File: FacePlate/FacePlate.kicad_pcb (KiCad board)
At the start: 4 copper layers, 131.1 x 44 mm, 50 parts, among them J2 GPIO, J3 Conn_01x04_Pin, U4 SX1280, U5 MCP2515-xST, U6 MCP2551-I-SN, U7 AMS1117-3.3, Y2 ABM3-8.000MHZ-D2Y-T

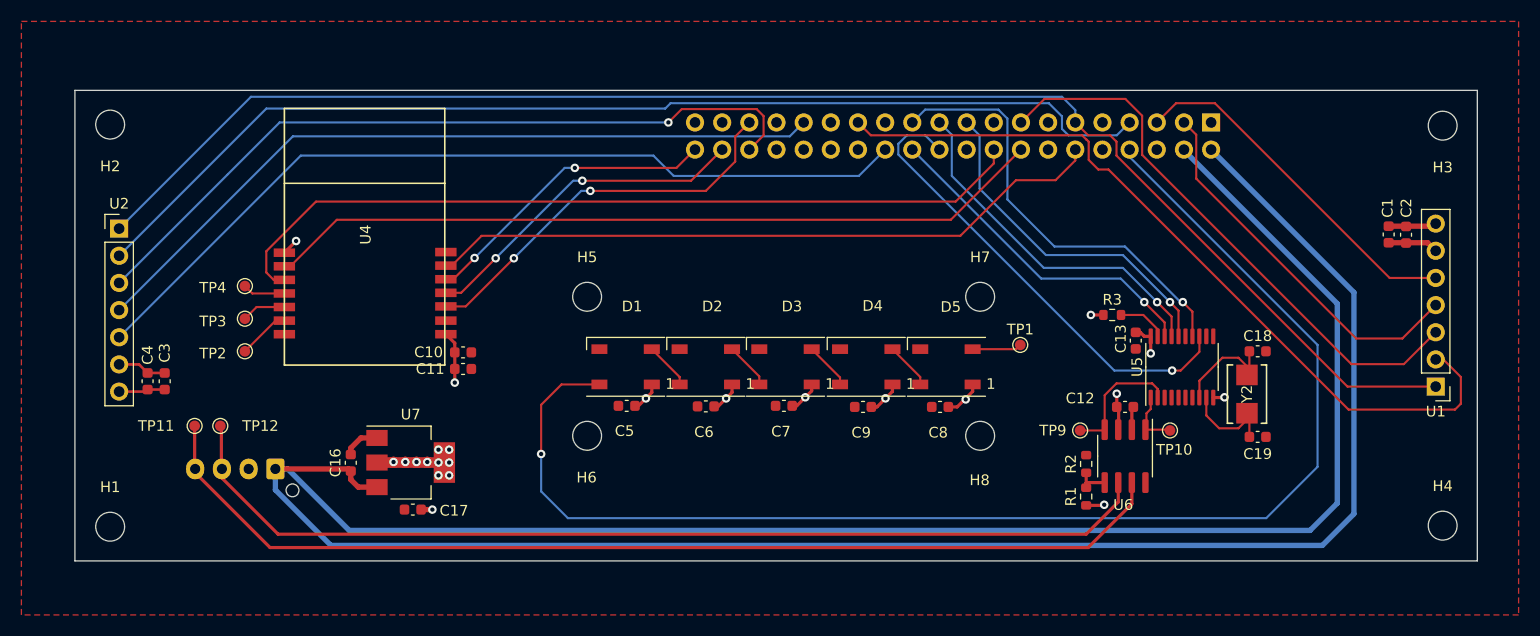
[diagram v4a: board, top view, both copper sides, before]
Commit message: update radio model
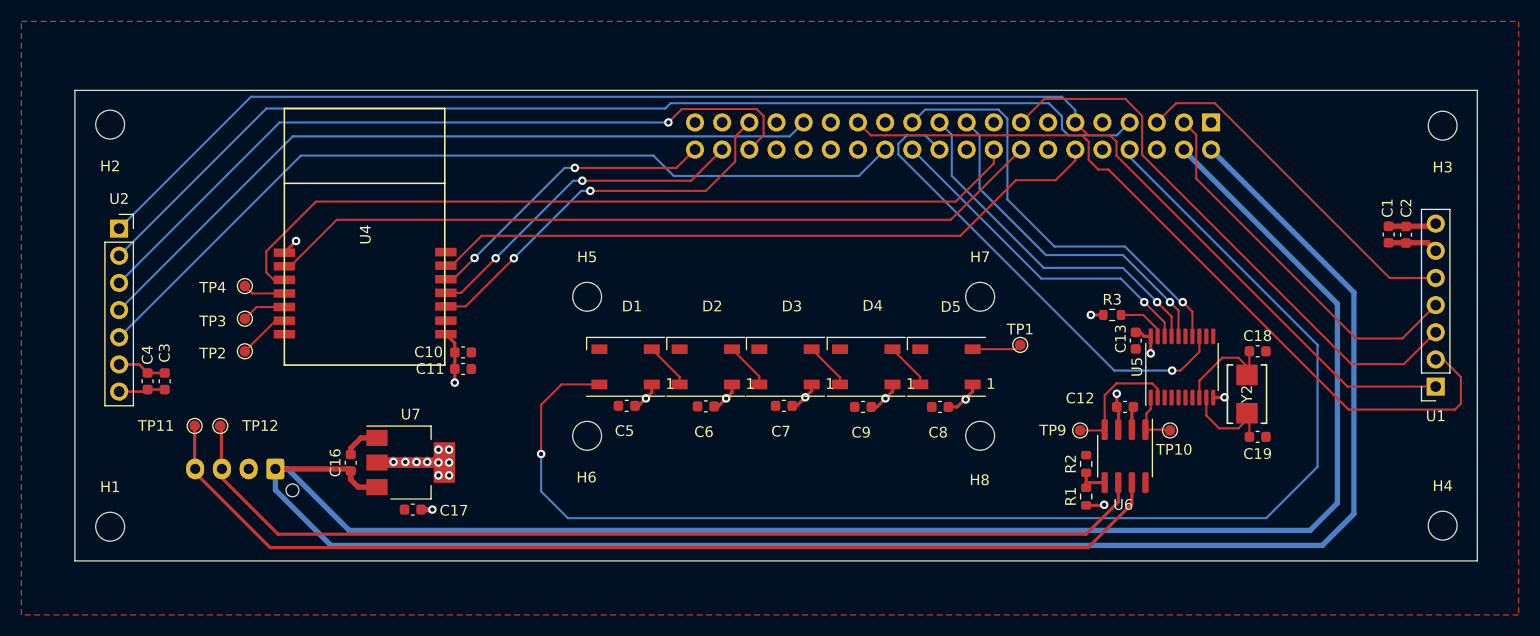
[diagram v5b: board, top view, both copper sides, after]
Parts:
- U1, U2: footprint Connector_PinHeader_2.54mm:PinHeader_1x07_P2.54mm_Vertical -> Connector_PinSocket_2.54mm:PinSocket_1x07_P2.54mm_Vertical
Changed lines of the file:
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@@
   (net 57 "/CAN/OSC2")
   (net 58 "/CAN/OSC1")
-  (footprint "Connector_PinHeader_2.54mm:PinHeader_1x07_P2.54mm_Vertical" (layer "F.Cu")
+  (footprint "Connector_PinSocket_2.54mm:PinSocket_1x07_P2.54mm_Vertical" (layer "F.Cu")
     (at 104.14 68.9256)
-    (descr "Through hole straight pin header, 1x07, 2.54mm pitch, single row")
-    (tags "Through hole pin header THT 1x07 2.54mm single row")
+    (descr "Through hole straight socket strip, 1x07, 2.54mm pitch, single row (from Kicad 4.0.7), script generated")
+    (tags "Through hole socket strip THT 1x07 2.54mm single row")
     (property "LCSC" "C718238")
     (property "Sheetfile" "FacePlate.kicad_sch")
     (property "Sheetname" "")
     (attr through_hole)
-    (fp_text reference "U2" (at 0 -2.33) (layer "F.SilkS")
-        (effects (font (size 1 1) (thickness 0.15)))
-    )
-    (fp_text value "~" (at 0 17.57) (layer "F.Fab")
+    (fp_text reference "U2" (at 0 -2.77) (layer "F.SilkS")
+        (effects (font (size 1 1) (thickness 0.15)))
+    )
+    (fp_text value "~" (at 0 18.01) (layer "F.Fab")
         (effects (font (size 1 1) (thickness 0.15)))
     )
@@
         (effects (font (size 1 1) (thickness 0.15)))
     )
-    (fp_line (start -1.33 -1.33) (end 0 -1.33)
-      (stroke (width 0.12) (type solid)) (layer "F.SilkS"))
-    (fp_line (start -1.33 0) (end -1.33 -1.33)
-      (stroke (width 0.12) (type solid)) (layer "F.SilkS"))
     (fp_line (start -1.33 1.27) (end -1.33 16.57)
       (stroke (width 0.12) (type solid)) (layer "F.SilkS"))
@@
     (fp_line (start -1.33 16.57) (end 1.33 16.57)
       (stroke (width 0.12) (type solid)) (layer "F.SilkS"))
+    (fp_line (start 0 -1.33) (end 1.33 -1.33)
+      (stroke (width 0.12) (type solid)) (layer "F.SilkS"))
+    (fp_line (start 1.33 -1.33) (end 1.33 0)
+      (stroke (width 0.12) (type solid)) (layer "F.SilkS"))
     (fp_line (start 1.33 1.27) (end 1.33 16.57)
       (stroke (width 0.12) (type solid)) (layer "F.SilkS"))
-    (fp_line (start -1.8 -1.8) (end -1.8 17.05)
-      (stroke (width 0.05) (type solid)) (layer "F.CrtYd"))
-    (fp_line (start -1.8 17.05) (end 1.8 17.05)
-      (stroke (width 0.05) (type solid)) (layer "F.CrtYd"))
-    (fp_line (start 1.8 -1.8) (end -1.8 -1.8)
-      (stroke (width 0.05) (type solid)) (layer "F.CrtYd"))
-    (fp_line (start 1.8 17.05) (end 1.8 -1.8)
-      (stroke (width 0.05) (type solid)) (layer "F.CrtYd"))
-    (fp_line (start -1.27 -0.635) (end -0.635 -1.27)
-      (stroke (width 0.1) (type solid)) (layer "F.Fab"))
-    (fp_line (start -1.27 16.51) (end -1.27 -0.635)
-      (stroke (width 0.1) (type solid)) (layer "F.Fab"))
-    (fp_line (start -0.635 -1.27) (end 1.27 -1.27)
-      (stroke (width 0.1) (type solid)) (layer "F.Fab"))
-    (fp_line (start 1.27 -1.27) (end 1.27 16.51)
+    (fp_line (start -1.8 -1.8) (end 1.75 -1.8)
+      (stroke (width 0.05) (type solid)) (layer "F.CrtYd"))
+    (fp_line (start -1.8 17) (end -1.8 -1.8)
+      (stroke (width 0.05) (type solid)) (layer "F.CrtYd"))
+    (fp_line (start 1.75 -1.8) (end 1.75 17)
+      (stroke (width 0.05) (type solid)) (layer "F.CrtYd"))
+    (fp_line (start 1.75 17) (end -1.8 17)
+      (stroke (width 0.05) (type solid)) (layer "F.CrtYd"))
+    (fp_line (start -1.27 -1.27) (end 0.635 -1.27)
+      (stroke (width 0.1) (type solid)) (layer "F.Fab"))
+    (fp_line (start -1.27 16.51) (end -1.27 -1.27)
+      (stroke (width 0.1) (type solid)) (layer "F.Fab"))
+    (fp_line (start 0.635 -1.27) (end 1.27 -0.635)
+      (stroke (width 0.1) (type solid)) (layer "F.Fab"))
+    (fp_line (start 1.27 -0.635) (end 1.27 16.51)
       (stroke (width 0.1) (type solid)) (layer "F.Fab"))
     (fp_line (start 1.27 16.51) (end -1.27 16.51)
@@
     (pad "7" thru_hole oval (at 0 15.24) (size 1.7 1.7) (drill 1) (layers "*.Cu" "*.Mask")
       (net 3 "+3.3V") (pinfunction "VCC") (pintype "power_in"))
-    (model "${KICAD6_3DMODEL_DIR}/Connector_PinHeader_2.54mm.3dshapes/PinHeader_1x07_P2.54mm_Vertical.wrl"
+    (model "${KICAD6_3DMODEL_DIR}/Connector_PinSocket_2.54mm.3dshapes/PinSocket_1x07_P2.54mm_Vertical.wrl"
       (offset (xyz 0 0 0))
       (scale (xyz 1 1 1))
@@
     )
   )
-  (footprint "Connector_PinHeader_2.54mm:PinHeader_1x07_P2.54mm_Vertical" (layer "F.Cu")
+  (footprint "Connector_PinSocket_2.54mm:PinSocket_1x07_P2.54mm_Vertical" (layer "F.Cu")
     (at 227.25 83.7 180)
-    (descr "Through hole straight pin header, 1x07, 2.54mm pitch, single row")
-    (tags "Through hole pin header THT 1x07 2.54mm single row")
+    (descr "Through hole straight socket strip, 1x07, 2.54mm pitch, single row (from Kicad 4.0.7), script generated")
+    (tags "Through hole socket strip THT 1x07 2.54mm single row")
     (property "LCSC" "C718238")
     (property "Sheetfile" "FacePlate.kicad_sch")
     (property "Sheetname" "")
     (attr through_hole)
-    (fp_text reference "U1" (at 0 -2.33) (layer "F.SilkS")
-        (effects (font (size 1 1) (thickness 0.15)))
-    )
-    (fp_text value "~" (at 0 17.57) (layer "F.Fab")
-        (effects (font (size 1 1) (thickness 0.15)))
-    )
-    (fp_text user "${REFERENCE}" (at 0 7.62 90) (layer "F.Fab")
-        (effects (font (size 1 1) (thickness 0.15)))
-    )
-    (fp_line (start -1.33 -1.33) (end 0 -1.33)
-      (stroke (width 0.12) (type solid)) (layer "F.SilkS"))
-    (fp_line (start -1.33 0) (end -1.33 -1.33)
-      (stroke (width 0.12) (type solid)) (layer "F.SilkS"))
+    (fp_text reference "U1" (at 0 -2.77 180) (layer "F.SilkS")
+        (effects (font (size 1 1) (thickness 0.15)))
+    )
+    (fp_text value "~" (at 0 18.01 180) (layer "F.Fab")
+        (effects (font (size 1 1) (thickness 0.15)))
+    )
+    (fp_text user "${REFERENCE}" (at 0 7.62 270) (layer "F.Fab")
+        (effects (font (size 1 1) (thickness 0.15)))
+    )
     (fp_line (start -1.33 1.27) (end -1.33 16.57)
       (stroke (width 0.12) (type solid)) (layer "F.SilkS"))
@@
     (fp_line (start -1.33 16.57) (end 1.33 16.57)
       (stroke (width 0.12) (type solid)) (layer "F.SilkS"))
+    (fp_line (start 0 -1.33) (end 1.33 -1.33)
+      (stroke (width 0.12) (type solid)) (layer "F.SilkS"))
+    (fp_line (start 1.33 -1.33) (end 1.33 0)
+      (stroke (width 0.12) (type solid)) (layer "F.SilkS"))
     (fp_line (start 1.33 1.27) (end 1.33 16.57)
       (stroke (width 0.12) (type solid)) (layer "F.SilkS"))
-    (fp_line (start -1.8 -1.8) (end -1.8 17.05)
-      (stroke (width 0.05) (type solid)) (layer "F.CrtYd"))
-    (fp_line (start -1.8 17.05) (end 1.8 17.05)
-      (stroke (width 0.05) (type solid)) (layer "F.CrtYd"))
-    (fp_line (start 1.8 -1.8) (end -1.8 -1.8)
-      (stroke (width 0.05) (type solid)) (layer "F.CrtYd"))
-    (fp_line (start 1.8 17.05) (end 1.8 -1.8)
-      (stroke (width 0.05) (type solid)) (layer "F.CrtYd"))
-    (fp_line (start -1.27 -0.635) (end -0.635 -1.27)
-      (stroke (width 0.1) (type solid)) (layer "F.Fab"))
-    (fp_line (start -1.27 16.51) (end -1.27 -0.635)
-      (stroke (width 0.1) (type solid)) (layer "F.Fab"))
-    (fp_line (start -0.635 -1.27) (end 1.27 -1.27)
-      (stroke (width 0.1) (type solid)) (layer "F.Fab"))
-    (fp_line (start 1.27 -1.27) (end 1.27 16.51)
+    (fp_line (start -1.8 -1.8) (end 1.75 -1.8)
+      (stroke (width 0.05) (type solid)) (layer "F.CrtYd"))
+    (fp_line (start -1.8 17) (end -1.8 -1.8)
+      (stroke (width 0.05) (type solid)) (layer "F.CrtYd"))
+    (fp_line (start 1.75 -1.8) (end 1.75 17)
+      (stroke (width 0.05) (type solid)) (layer "F.CrtYd"))
+    (fp_line (start 1.75 17) (end -1.8 17)
+      (stroke (width 0.05) (type solid)) (layer "F.CrtYd"))
+    (fp_line (start -1.27 -1.27) (end 0.635 -1.27)
+      (stroke (width 0.1) (type solid)) (layer "F.Fab"))
+    (fp_line (start -1.27 16.51) (end -1.27 -1.27)
+      (stroke (width 0.1) (type solid)) (layer "F.Fab"))
+    (fp_line (start 0.635 -1.27) (end 1.27 -0.635)
+      (stroke (width 0.1) (type solid)) (layer "F.Fab"))
+    (fp_line (start 1.27 -0.635) (end 1.27 16.51)
       (stroke (width 0.1) (type solid)) (layer "F.Fab"))
     (fp_line (start 1.27 16.51) (end -1.27 16.51)
@@
     (pad "7" thru_hole oval (at 0 15.24 180) (size 1.7 1.7) (drill 1) (layers "*.Cu" "*.Mask")
       (net 3 "+3.3V") (pinfunction "VCC") (pintype "power_in"))
-    (model "${KICAD6_3DMODEL_DIR}/Connector_PinHeader_2.54mm.3dshapes/PinHeader_1x07_P2.54mm_Vertical.wrl"
+    (model "${KICAD6_3DMODEL_DIR}/Connector_PinSocket_2.54mm.3dshapes/PinSocket_1x07_P2.54mm_Vertical.wrl"
       (offset (xyz 0 0 0))
       (scale (xyz 1 1 1))
@@
     (pad "14" smd rect (at -9.31 -7.6 90) (size 0.8 2) (layers "F.Cu" "F.Paste" "F.Mask")
       (net 1 "GND") (pinfunction "GND") (pintype "power_in"))
+    (model "${KIPRJMOD}/3d_models/E28-2G4M27S.STEP"
+      (offset (xyz 0 26.5 3))
+      (scale (xyz 1 1 1))
+      (rotate (xyz -90 0 0))
+    )
   )
   (footprint "Resistor_SMD:R_0603_1608Metric" (layer "F.Cu")

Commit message: finalize with 0ohms
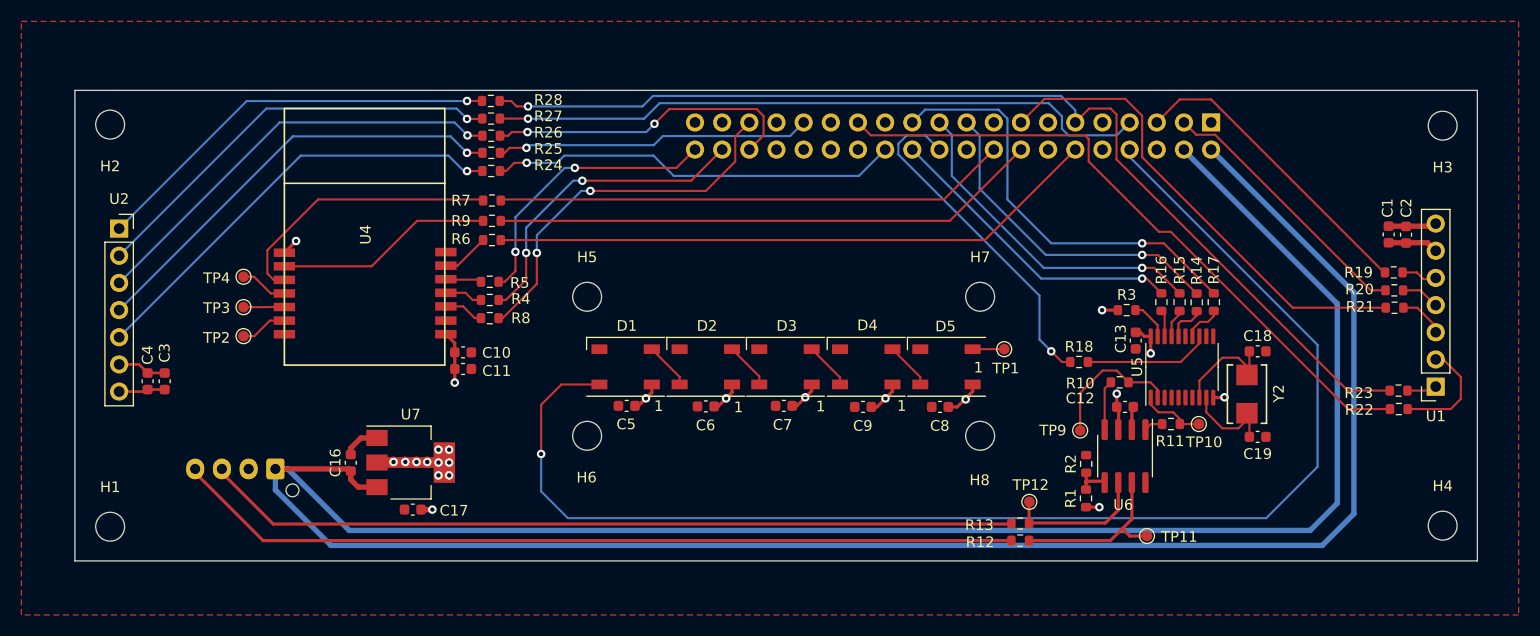
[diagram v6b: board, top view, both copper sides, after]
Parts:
- added R10: 0k, Resistor_SMD:R_0603_1608Metric, F.Cu at (197.7, 83.3)
- added R11: 0k, Resistor_SMD:R_0603_1608Metric, F.Cu at (202.5, 87.2)
- added R12: 0k, Resistor_SMD:R_0603_1608Metric, F.Cu at (188.4, 98.1)
- added R13: 0k, Resistor_SMD:R_0603_1608Metric, F.Cu at (188.4, 96.5)
- added R14: 0k, Resistor_SMD:R_0603_1608Metric, F.Cu at (204.9, 75.8)
- added R15: 0k, Resistor_SMD:R_0603_1608Metric, F.Cu at (203.3, 75.8)
- added R16: 0k, Resistor_SMD:R_0603_1608Metric, F.Cu at (201.6, 75.8)
- added R17: 0k, Resistor_SMD:R_0603_1608Metric, F.Cu at (206.5, 75.8)
- added R18: 0k, Resistor_SMD:R_0603_1608Metric, F.Cu at (193.9, 81.4)
- added R19: 0k, Resistor_SMD:R_0603_1608Metric, F.Cu at (223.3, 73.0)
- added R20: 0k, Resistor_SMD:R_0603_1608Metric, F.Cu at (223.4, 74.7)
- added R21: 0k, Resistor_SMD:R_0603_1608Metric, F.Cu at (223.4, 76.3)
- added R22: 0k, Resistor_SMD:R_0603_1608Metric, F.Cu at (223.8, 85.8)
- added R23: 0k, Resistor_SMD:R_0603_1608Metric, F.Cu at (223.8, 84.1)
- added R24: 0k, Resistor_SMD:R_0603_1608Metric, F.Cu at (138.9, 63.5)
- added R25: 0k, Resistor_SMD:R_0603_1608Metric, F.Cu at (138.9, 61.8)
- added R26: 0k, Resistor_SMD:R_0603_1608Metric, F.Cu at (138.9, 60.2)
- added R27: 0k, Resistor_SMD:R_0603_1608Metric, F.Cu at (138.9, 58.6)
- added R28: 0k, Resistor_SMD:R_0603_1608Metric, F.Cu at (138.9, 57.0)
- added R4: 0k, Resistor_SMD:R_0603_1608Metric, F.Cu at (138.8, 75.6)
- added R5: 0k, Resistor_SMD:R_0603_1608Metric, F.Cu at (138.8, 73.9)
- added R6: 0k, Resistor_SMD:R_0603_1608Metric, F.Cu at (139.0, 70.0)
- added R7: 0k, Resistor_SMD:R_0603_1608Metric, F.Cu at (139.0, 66.3)
- added R8: 0k, Resistor_SMD:R_0603_1608Metric, F.Cu at (138.8, 77.3)
- added R9: 0k, Resistor_SMD:R_0603_1608Metric, F.Cu at (139.0, 68.2)
- moved TP11 89.6 mm to (200.2, 97.7)
- moved TP12 76.0 mm to (189.2, 94.5)
- moved TP10 2.77 mm to (205.1, 87.2)
- moved TP1 1.55 mm to (186.9, 80.2)
- moved TP2 1.43 mm to (115.8, 79.0)
- moved R3 1.42 mm to (198.3, 76.5)
- moved TP3 1.09 mm to (115.8, 76.3)
- moved TP4 0.88 mm to (115.8, 73.4)
- moved R1 0.17 mm to (194.6, 94.2)
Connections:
- TP11 pad 1: /CAN/CAN_H -> Net-(U6-CANH)
- TP12 pad 1: /CAN/CAN_L -> Net-(U6-CANL)
- U1 pad 1: /GPIO[17] -> Net-(U1-RST)
- U1 pad 2: /SPI3_NSS -> Net-(U1-CS)
- U1 pad 3: /GPIO[22] -> Net-(U1-DC)
- U1 pad 4: /SPI3_MOSI -> Net-(U1-MOSI)
- U1 pad 5: /SPI3_SCLK -> Net-(U1-CLK)
- U2 pad 1: /GPIO[17] -> Net-(U2-RST)
- U2 pad 2: /SPI4_NSS -> Net-(U2-CS)
- U2 pad 3: /GPIO[16] -> Net-(U2-DC)
- U2 pad 4: /SPI4_MOSI -> Net-(U2-MOSI)
- U2 pad 5: /SPI4_CLK -> Net-(U2-CLK)
- U4 pad 10: /GPIO[24] -> Net-(U4-BUSY)
- U4 pad 3: /SPI6_MISO -> Net-(U4-MISO)
- U4 pad 4: /SPI6_MOSI -> Net-(U4-MOSI)
- U4 pad 5: /SPI6_SCLK -> Net-(U4-SCK)
- U4 pad 6: /SPI6_NSS -> Net-(U4-NSS)
- U4 pad 9: /GPIO[23] -> Net-(U4-nReset)
- U5 pad 13: /GPIO[25] -> Net-(U5-~{INT})
- U5 pad 14: /SPI0_SCLK -> Net-(U5-SCK)
- U5 pad 16: /SPI0_MOSI -> Net-(U5-SI)
- U5 pad 17: /SPI0_MISO -> Net-(U5-SO)
- U5 pad 18: /SPI0_NSS -> Net-(U5-~{CS})
- U6 pad 1: /CAN/TXCAN -> Net-(U6-TXD)
- U6 pad 4: /CAN/RXCAN -> Net-(U6-RXD)
- U6 pad 6: /CAN/CAN_L -> Net-(U6-CANL)
- U6 pad 7: /CAN/CAN_H -> Net-(U6-CANH)
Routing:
- net /SPI4_CLK: track 80.5 -> 38.4 mm, vias 0 -> 1
- net Net-(U2-MOSI): track 0.00 -> 41.7 mm, vias 0 -> 1
- net /SPI4_MOSI: track 71.3 -> 29.7 mm, vias 0 -> 1
- net /GPIO[17]: track 140.9 -> 99.5 mm, vias 0 -> 1
- net /GPIO[16]: track 71.0 -> 29.6 mm, vias 1 -> 2
- net Net-(U2-CLK): track 0.00 -> 41.3 mm, vias 0 -> 1
- net /SPI4_NSS: track 102.8 -> 61.9 mm, vias 0 -> 1
- net Net-(U2-DC): track 0.00 -> 40.7 mm, vias 0 -> 1
- net Net-(U2-CS): track 0.00 -> 40.1 mm, vias 0 -> 1
- net Net-(U2-RST): track 0.00 -> 38.9 mm, vias 0 -> 1
- net /GPIO[24]: track 76.7 -> 48.1 mm
- net Net-(U4-BUSY): track 0.00 -> 26.2 mm
- net /GPIO[23]: track 73.4 -> 51.4 mm
- net Net-(U4-nReset): track 0.00 -> 20.3 mm
- net /CAN/CAN_H: track 98.7 -> 79.4 mm
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
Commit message: faceplate modifications
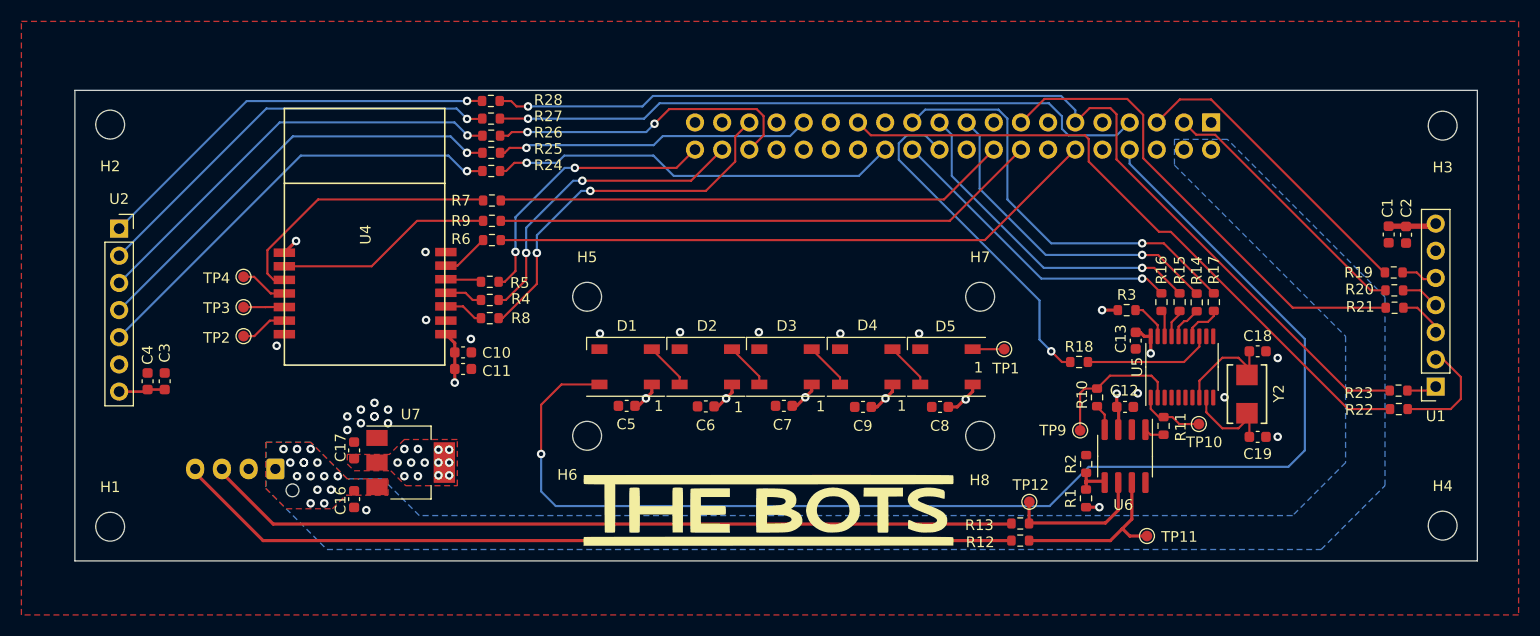
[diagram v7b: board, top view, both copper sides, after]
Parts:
- added G***: LOGO, LOGO, F.Cu at (164.8, 95.2)
- moved C17 7.80 mm to (126.1, 89.7), turned to 90 degrees
- moved C16 3.41 mm to (126.1, 94.2), turned to -90 degrees
- moved R10 2.55 mm to (195.6, 84.7), turned to 90 degrees
- moved R11 0.72 mm to (201.8, 87.4), turned to 90 degrees
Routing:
- net +5V: track 298.2 -> 0.00 mm, vias 0 -> 15
- net GND: track 19.1 -> 2.40 mm, vias 2 -> 24
- net +3.3V: track 47.2 -> 38.7 mm, vias 21 -> 23
- net /SPI5_MOSI: track 126.9 -> 123.4 mm
- net Net-(U6-RXD): track 4.27 -> 2.49 mm
- added copper zone on F.Cu, net +3.3V
- added copper zone on In1.Cu, net +3.3V
- added copper zone on B.Cu, net +5V
- added copper zone on F.Cu, net +5V
- added copper zone on In2.Cu, net GND
- removed copper zone on In2.Cu, net +3.3V
- removed copper zone on In1.Cu, net GND
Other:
- board text added: "The Bots Faceplate Designed by Akhil V January 30, 2024"
- board text removed: "The Bots Faceplate Designed by Akhil V"
